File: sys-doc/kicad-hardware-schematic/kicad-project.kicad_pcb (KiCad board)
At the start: 2 copper layers, 66.7 x 65.3 mm, 7 parts, among them J1 DHT11 (Temp/Hum), SW1 Switch (CollectTraining), SW2 Switch (IsOutlier), U1 ESP32-DevKitC

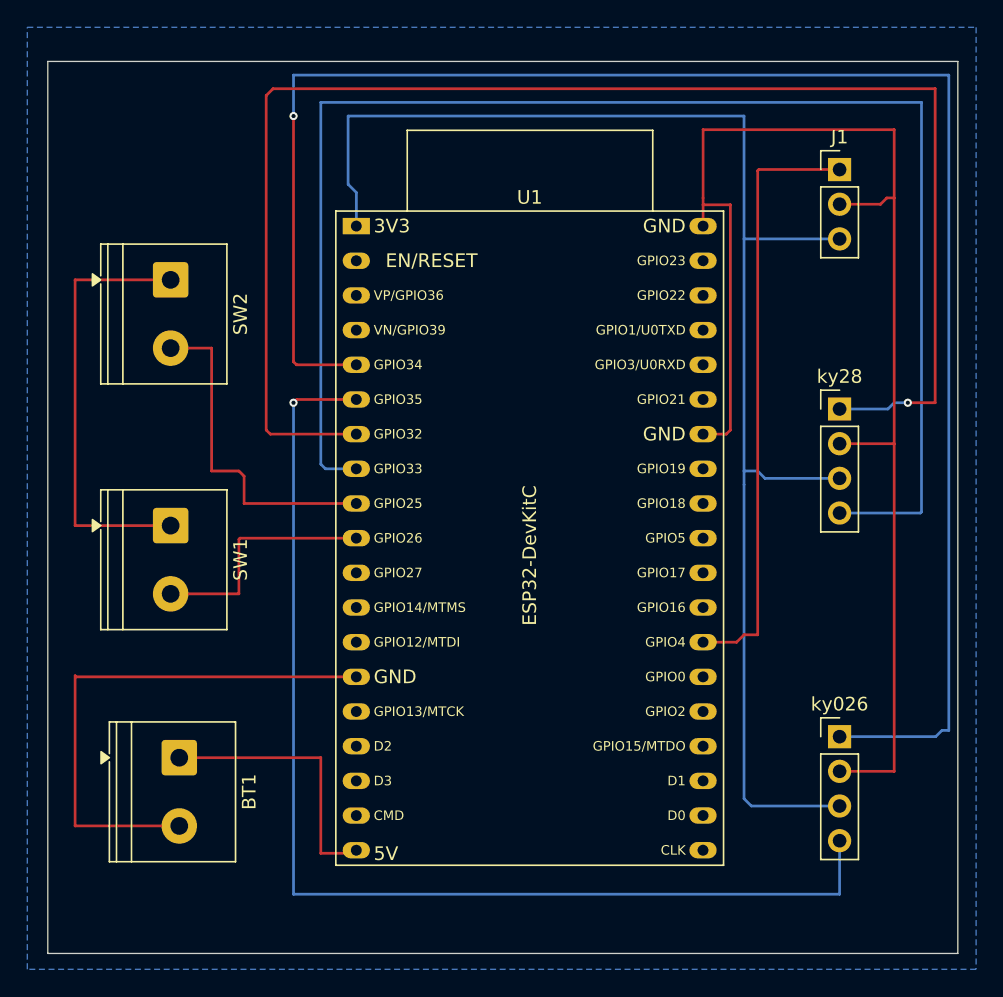
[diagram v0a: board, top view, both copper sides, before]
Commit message: Prepare and do pdf export of KiCAD project
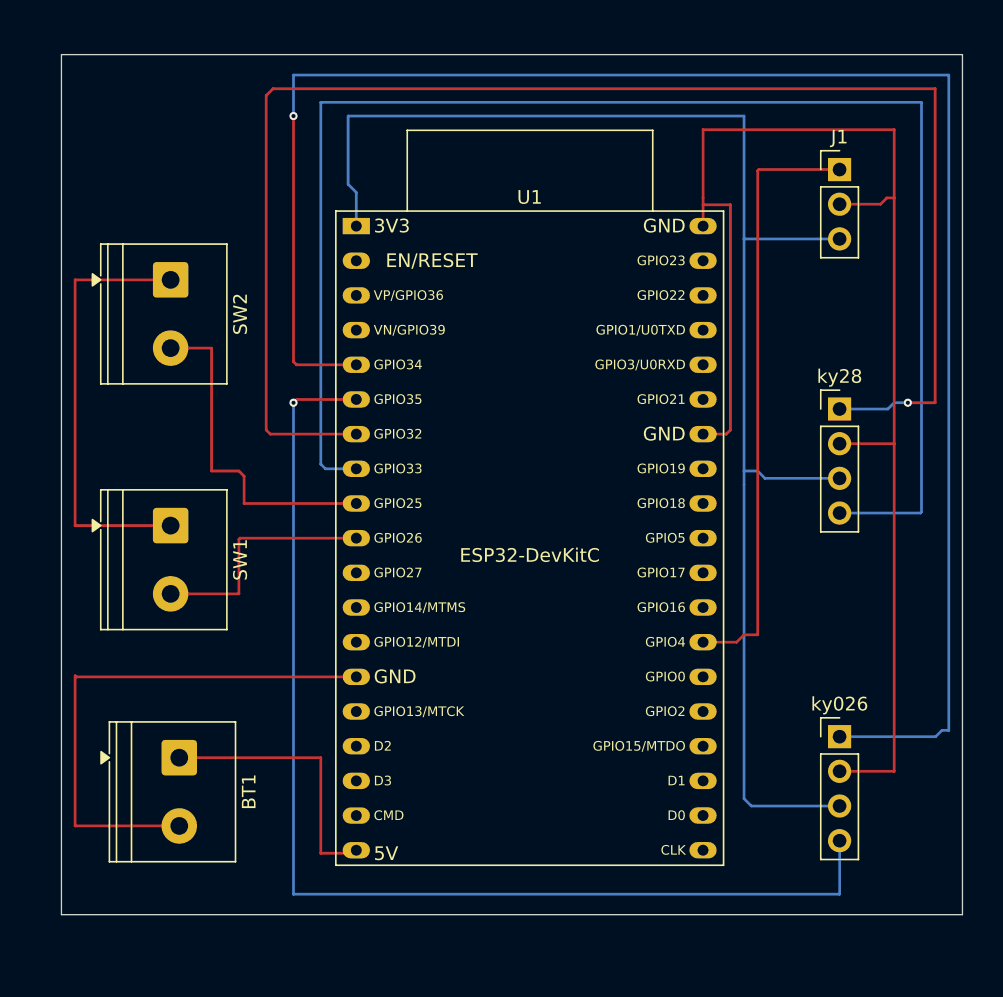
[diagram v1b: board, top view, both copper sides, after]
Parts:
- BT1: value Stromversorgung -> Battery
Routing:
- removed copper zone on B.Cu, net /GND
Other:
- board size 66.7 x 65.3 mm -> 66 x 63 mm
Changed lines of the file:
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@@
 		(filling no)
 		(pcbplotparams
-			(layerselection 0x00000000_00000000_55555555_5755f5ff)
+			(layerselection 0x00000000_00000000_55555555_57555555)
 			(plot_on_all_layers_selection 0x00000000_00000000_00000000_00000000)
 			(disableapertmacros no)
@@
 			(psnegative no)
 			(psa4output no)
-			(plot_black_and_white yes)
+			(plot_black_and_white no)
 			(sketchpadsonfab no)
 			(plotpadnumbers no)
@@
 			(crossoutdnponfab yes)
 			(subtractmaskfromsilk no)
-			(outputformat 1)
+			(outputformat 4)
 			(mirror no)
 			(drillshape 0)
 			(scaleselection 1)
-			(outputdirectory "fabrication_plotter")
+			(outputdirectory "fabrication_plotter_pdf")
 		)
 	)
@@
 		)
 		(property "Value" "DHT11 (Temp/Hum)"
-			(at 0 7.46 0)
+			(at 0.5 8.08 0)
 			(layer "F.Fab")
 			(effects
@@
 		)
 		(property "Value" "KY-028 (Thermistor)"
-			(at 0 10 0)
+			(at 0.5 11.04 0)
 			(layer "F.Fab")
 			(effects
@@
 		)
 		(property "Value" "KY-026 (Flame)"
-			(at 0 10 0)
+			(at 0.5 10.54 0)
 			(layer "F.Fab")
 			(effects
@@
 		)
 		(property "Value" "ESP32-DevKitC"
-			(at 12.7 24.13 90)
+			(at 12.7 24.13 180)
 			(layer "F.SilkS")
 			(effects
@@
 		)
 		(property "Value" "Switch (IsOutlier)"
-			(at 2.5 6.12 90)
+			(at 9 0.5 180)
 			(layer "F.Fab")
 			(effects
@@
 			)
 		)
-		(property "Value" "Stromversorgung"
-			(at 2.5 6.12 90)
+		(property "Value" "Battery"
+			(at 9 0.1325 180)
 			(layer "F.Fab")
 			(effects
@@
 		)
 		(property "Value" "Switch (CollectTraining)"
-			(at 2.5 6.12 90)
+			(at 9 -1.5 180)
 			(layer "F.Fab")
 			(effects
@@
 	)
 	(gr_rect
-		(start 59 62)
-		(end 125.662451 127.339973)
+		(start 60 61.5)
+		(end 125.999999 124.499999)
 		(stroke
 			(width 0.05)
@@
 		(net "Net-(BT1-+)")
 	)
-	(zone
-		(net "/GND")
-		(layer "B.Cu")
-		(name "GroundNet")
-		(hatch edge 0.5)
-		(connect_pads
-			(clearance 0.5)
-		)
-		(min_thickness 0.25)
-		(fill yes
-			(thermal_gap 0.5)
-			(thermal_bridge_width 0.5)
-			(island_removal_mode 0)
-		)
-		(polygon
-			(pts
-				(xy 127 128.5) (xy 57.5 128.5) (xy 57.5 59.5) (xy 127 59.5)
-			)
-		)
-	)
 	(embedded_fonts no)
